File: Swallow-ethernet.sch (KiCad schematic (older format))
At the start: 39 parts, among them P1 XTAG2, P2 XMP16_TR_Link, P3 JTAG_Config, P4 TR_Link_Out, P5 Mode_Select, P9 JTAG_Loop, U1 25MHz_ASE_CLK, U15 NC7WZ17, U16 NC7WZ17, U17 NC7WZ17, U18 4k7, U19 4k7, U2 74LCX257, U3 33R, U4 33R, U5 74LCX257, U6 NC7WZ07, U7 NC7WZ07

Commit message: Created pinout for SDRAM + ethernet I/O board. Pushed pinout to schematic.
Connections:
- net labels added: XLC0i, XLC0o, XLC1i, XLC1o
- net labels removed: XLB0i, XLB0o, XLB1i, XLB1o
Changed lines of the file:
@@
-EESchema Schematic File Version 2  date 29/09/2012 20:57:41
+EESchema Schematic File Version 2  date 30/09/2012 20:10:30
 LIBS:power
 LIBS:device
@@
 Sheet 1 4
 Title "noname.sch"
-Date "29 sep 2012"
+Date "30 sep 2012"
 Rev ""
 Comp ""
@@
 TDO_XTAG
 Text Label 5130 2360 2    60   ~ 0
-XLB1o
+XLC1o
 Text Label 5130 2460 2    60   ~ 0
-XLB0o
+XLC0o
 Text Label 5790 2860 2    60   ~ 0
-XLB1i
+XLC1i
 Text Label 5790 2760 2    60   ~ 0
-XLB0i
+XLC0i
 $Comp
 L GND #PWR08
@@
 F8 "RST_N" I L 5960 4060 60
 F9 "XLD0o" O R 7510 2760 60
-F10 "XLB0o" O L 5960 2460 60
-F11 "XLB1o" O L 5960 2360 60
-F12 "XLB2o" O L 5960 2260 60
-F13 "XLB3o" O L 5960 2160 60
-F14 "XLB4o" O L 5960 2060 60
-F15 "XLB1i" I L 5960 2860 60
-F16 "XLB0i" I L 5960 2760 60
-F17 "XLB4i" I L 5960 3160 60
-F18 "XLB3i" I L 5960 3060 60
-F19 "XLB2i" I L 5960 2960 60
-F20 "XLD1o" O R 7510 2860 60
-F21 "XLD2o" O R 7510 2960 60
-F22 "XLD3o" O R 7510 3060 60
-F23 "XLD4o" O R 7510 3160 60
-F24 "XLD4i" I R 7510 2240 60
-F25 "XLD3i" I R 7510 2340 60
-F26 "XLD2i" I R 7510 2430 60
-F27 "XLD1i" I R 7510 2520 60
-F28 "XLD0i" I R 7510 2610 60
-F29 "GPIO2" B R 7510 4120 60
-F30 "GPIO1" B R 7510 3760 60
+F10 "XLD1o" O R 7510 2860 60
+F11 "XLD2o" O R 7510 2960 60
+F12 "XLD3o" O R 7510 3060 60
+F13 "XLD4o" O R 7510 3160 60
+F14 "XLD4i" I R 7510 2240 60
+F15 "XLD3i" I R 7510 2340 60
+F16 "XLD2i" I R 7510 2430 60
+F17 "XLD1i" I R 7510 2520 60
+F18 "XLD0i" I R 7510 2610 60
+F19 "GPIO2" B R 7510 4120 60
+F20 "GPIO1" B R 7510 3760 60
+F21 "XLC0o" O L 5960 2450 60
+F22 "XLC1o" O L 5960 2350 60
+F23 "XLC2o" O L 5960 2250 60
+F24 "XLC3o" O L 5960 2150 60
+F25 "XLC4o" O L 5960 2050 60
+F26 "XLC4i" I L 5960 3150 60
+F27 "XLC3i" I L 5960 3050 60
+F28 "XLC2i" I L 5960 2950 60
+F29 "XLC1i" I L 5960 2850 60
+F30 "XLC0i" I L 5960 2750 60
 $EndSheet
 $Comp

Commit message: Completed schematic.
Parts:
- removed C4: 100n, SM0603, symbol C
- removed D1: JTAG_Loop, X_LED-0603, symbol LED
- removed P3: JTAG_Config, SIL-2, symbol CONN_2
- removed P9: JTAG_Loop, symbol CONN_2
- removed R5: 82R, SM0402, symbol R
- removed R6: 4k7, SM0402, symbol R
- removed U15, U16, U17: NC7WZ17, SC70-6, symbol NC7WZ17
- removed U2, U5: 74LCX257, TSSOP16, symbol 74LCX157
- removed W16: XLD2o, TestPad-1mm, symbol TESTPOINT
- removed W17: XLD30, TestPad-1mm, symbol TESTPOINT
- removed W18: XLD4o, TestPad-1mm, symbol TESTPOINT
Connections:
- net labels removed: A10, A11, A12, BR_THROUGH_3i, BR_THROUGH_4i, DEBUG_N_R, JTAG_Select, TCK_L, TCK_L1, TCK_R, TDI_L, TDI_L1, TDI_R, TDO_L, TDO_L1, TDO_R, TMS_L, TMS_L1, TMS_R
- wire segments 259 -> 213
- no-connect marks 5 -> 4
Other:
- note removed: "0 => L->Pass through->R ; XTAG<->L1\n1 => L->L1->R"
- note removed: "Boot from LinkB"
- note removed: "Loop JTAG if this is th\n last board in the chain"
- note removed: "MUX Decoupler"
- note removed: "May wish to disconnect\n this XTAG connection\nto prevent shorts"
- note removed: "TDI/TDO are enabled/disabled by XMP-16 board setting."

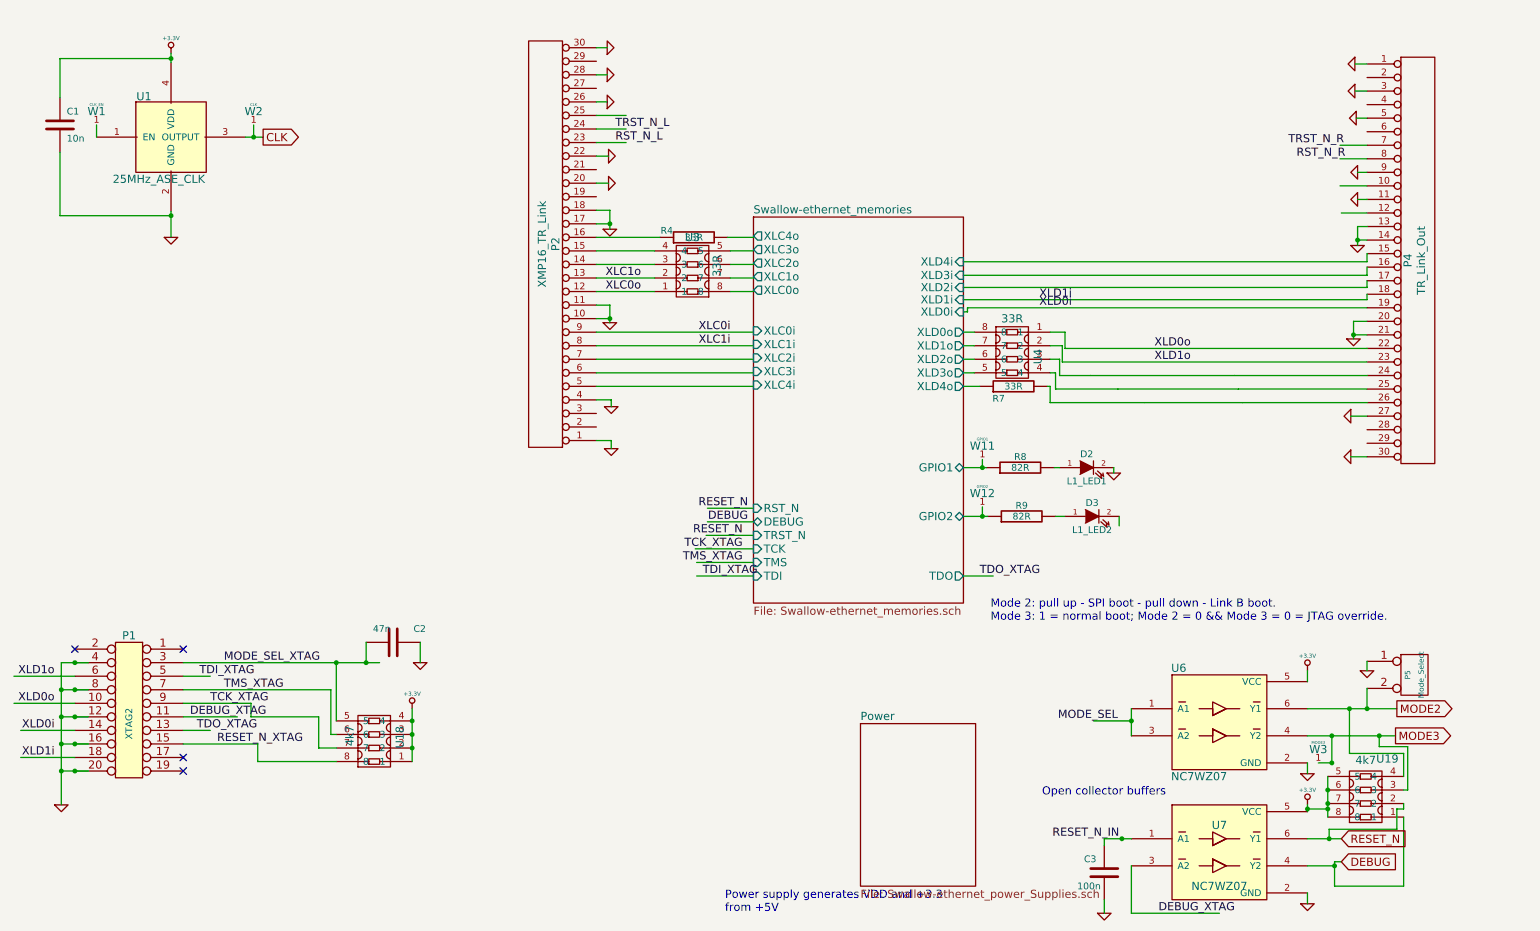
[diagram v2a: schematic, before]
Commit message: Re-annotated schematic and deleted redundant components from PCB design.
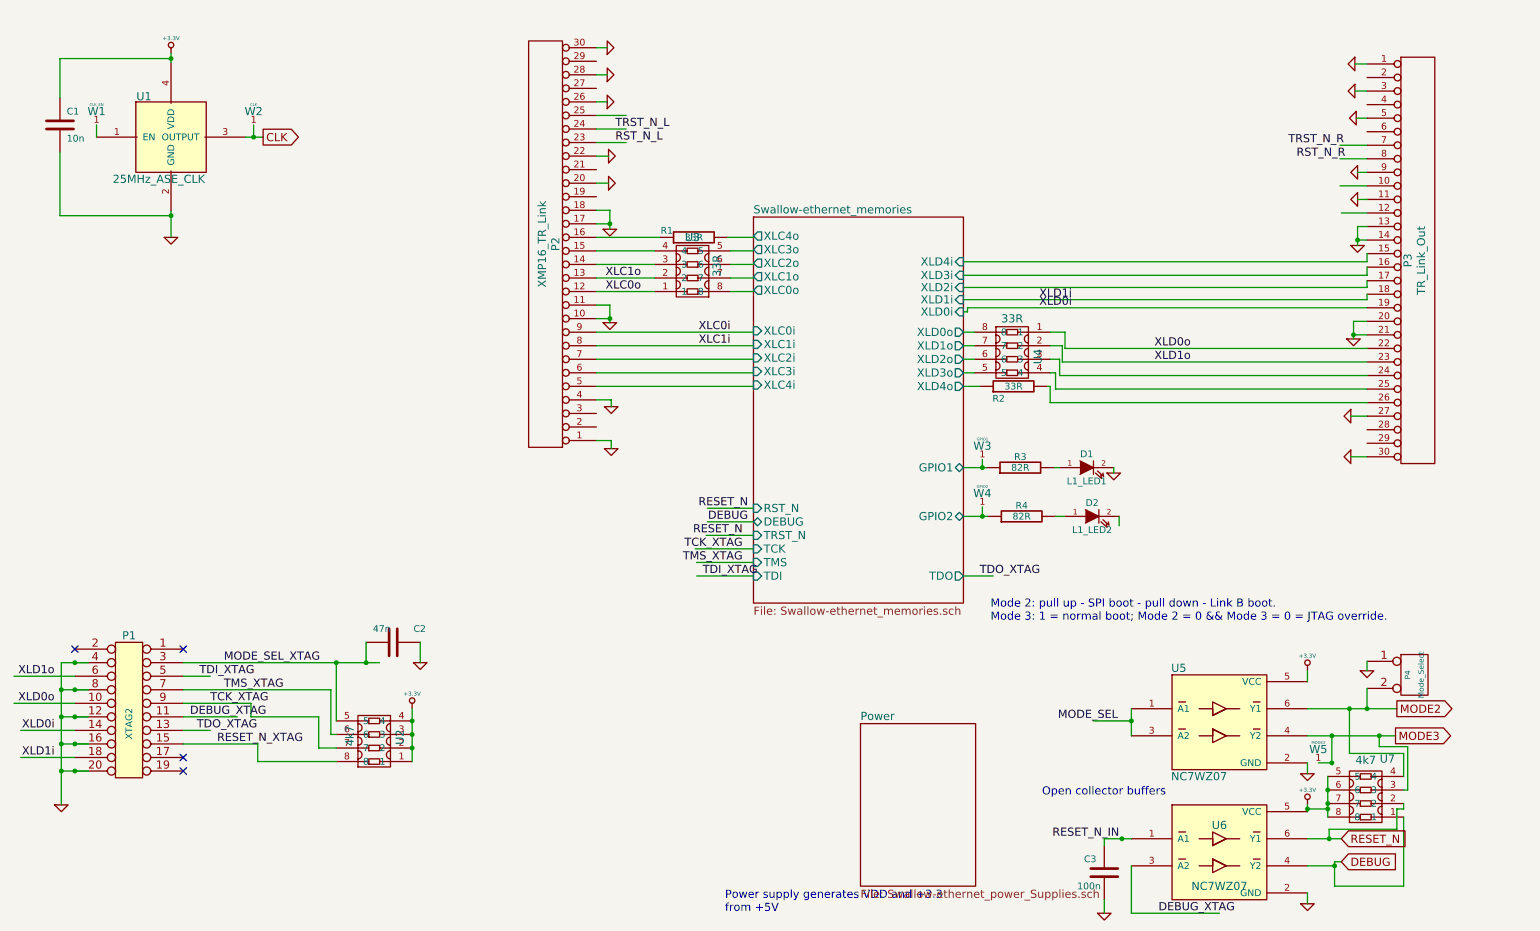
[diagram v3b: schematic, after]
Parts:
- renumbered D2 to D1, D3 to D2, P4 to P3, P5 to P4, R4 to R1, R7 to R2, R8 to R3, R9 to R4, U18 to U2, U6 to U5, U7 to U6, U19 to U7, W11 to W3, W12 to W4, W3 to W5
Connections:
- wire segments 213 -> 171
